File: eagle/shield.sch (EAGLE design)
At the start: 37 parts, among them Q1 REG1117, U1 TXB0104PWR, U2 TXB0104PWR

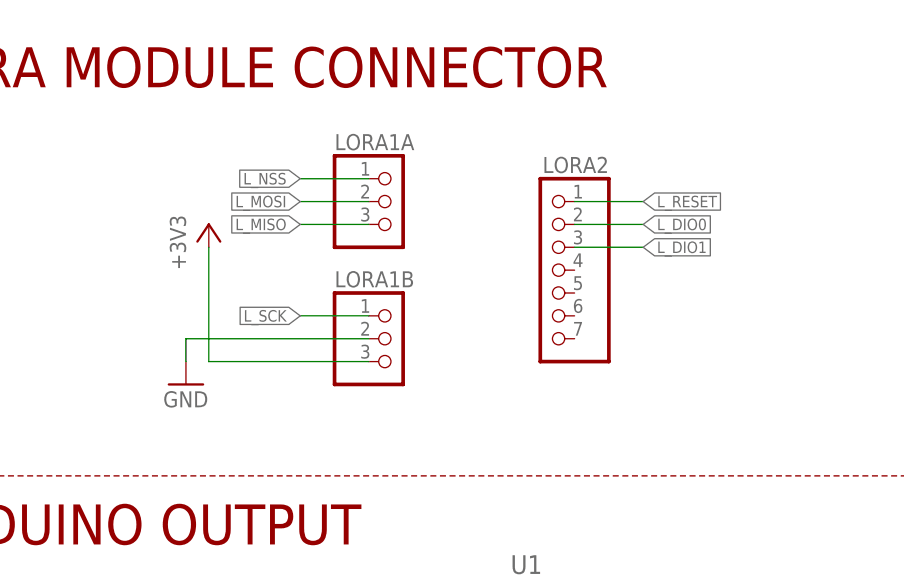
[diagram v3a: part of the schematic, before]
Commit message: Major layout update, read details
The layouts of shield and all breakout boards were changed to match the new multiprotocol standard.
IMPORTANT: The new shield is NOT compatible with the old breakout boards!
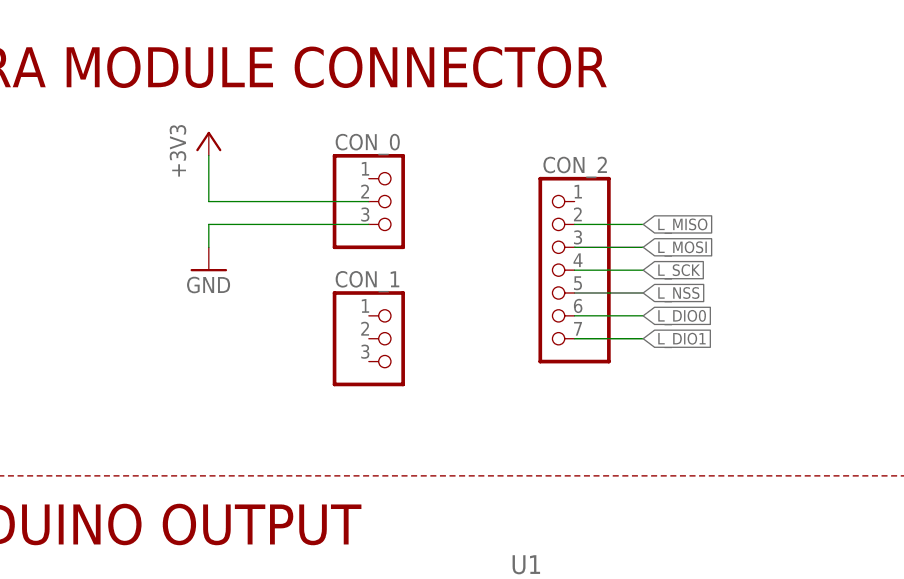
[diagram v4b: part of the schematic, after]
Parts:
- renumbered LORA1A to CON_0, LORA1B to CON_1, LORA2 to CON_2
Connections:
- net +3V3: now also CON_0.2; no longer CON_1.3
- net GND: now also CON_0.3; no longer CON_1.2
- net L_DIO0: now also CON_2.6; no longer CON_2.2
- net L_DIO1: now also CON_2.7; no longer CON_2.3
- net L_MISO: now also CON_2.2; no longer CON_0.3
- net L_MOSI: now also CON_2.3; no longer CON_0.2
- net L_NSS: now also CON_2.5; no longer CON_0.1
- net L_RESET: no longer CON_2.1
- net L_SCK: now also CON_2.4; no longer CON_1.1
